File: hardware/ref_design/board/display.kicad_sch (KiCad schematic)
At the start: 12 parts, among them J3 FH12-50S-0.5SH(55), U6 AP3156FVG-7

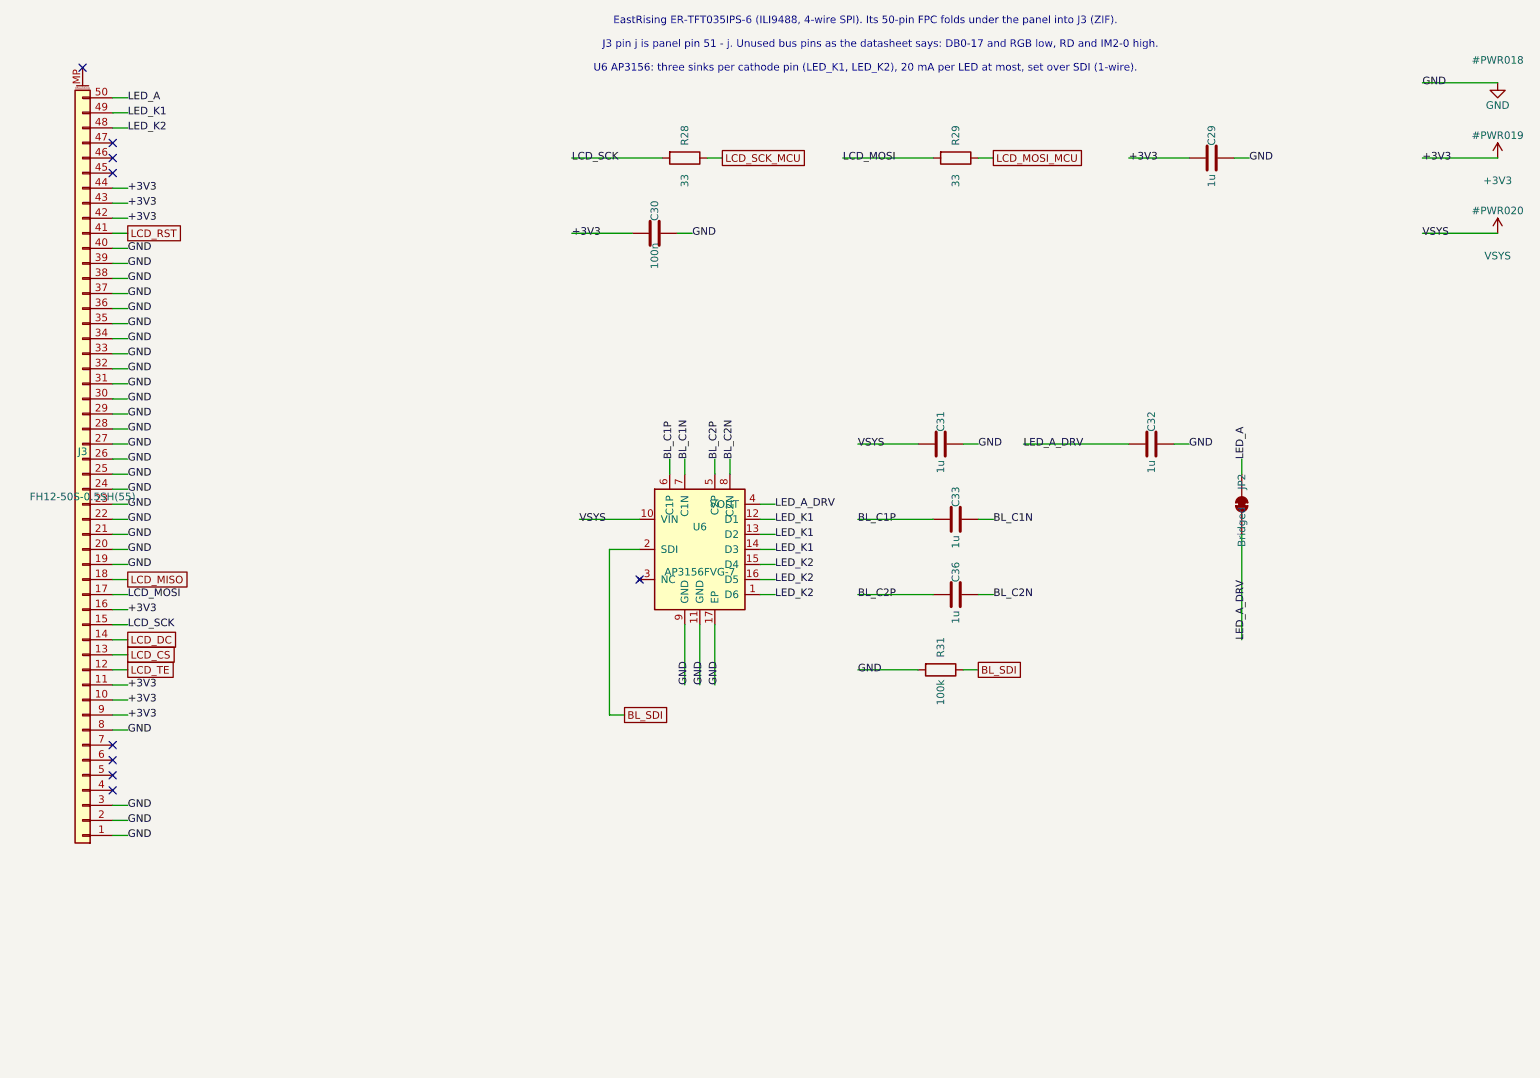
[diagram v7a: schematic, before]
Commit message: Reference design: discrete backlight current sinks replace the AP3156
The AP3156 charge pump (U6, C443652) is out of stock at JLC and LCSC. Each
of the panel's two cathode pins now has its own linear current sink: half
of an MCP6002 (U6, C7377 Preferred) drives an AO3400A (Q5/Q6, C20917 Basic)
and holds a 2.2 ohm sense resistor (R52/R53) at BL_REF. LED_A is on VSYS
through JP2. GPIO44 (now BL_PWM, PWM10 A) sets BL_REF through 100k/3.9k
and 1 uF: 0.124 V at 100% = 56 mA a pin, 113 mA in all (panel max 120).
RG 330 ohm, RF 10k, CF 1 nF, gate pull-downs 100k: simulated first
(board/sim, previous commit), phase margin >= 72.5 deg at every corner.

Every new part is Basic or Preferred: 12 extended part numbers instead of
13, parts $4.77 a board instead of $5.01, about $16.81 a unit at 10.

Layout: the sinks sit above J3's LED pins between J3 and J2, clear of the
ground bar route.py lays over J3's grounded pins; board rebuilt and
re-routed (route.py, 80 passes): DRC 0 errors, 0 unconnected, 0 parity,
2 cosmetic warnings as before. check_netlist, check_pins (29 parts, 244
pins, 94 passives), ERC 0, check_fit pass. silk.py puts J2's BATT label
above it (the op-amp is now on its left).

Docs: pin reviews for U6 and Q5/Q6 with page cites, passives, U4 (GPIO44)
and the panel; pinmap (GPIO44 PWM, backlight section), bring-up step 5,
design review, PLAN (also: the USB series resistors are 27 ohm, not 22),
BOM, assembly, validation plan items, SOURCES.

Co-Authored-By: Claude Opus 5.5 <noreply@anthropic.com>
Claude-Session: https://claude.ai/code/session_01Ceq1EsbekLwXHokcQ73Ldk
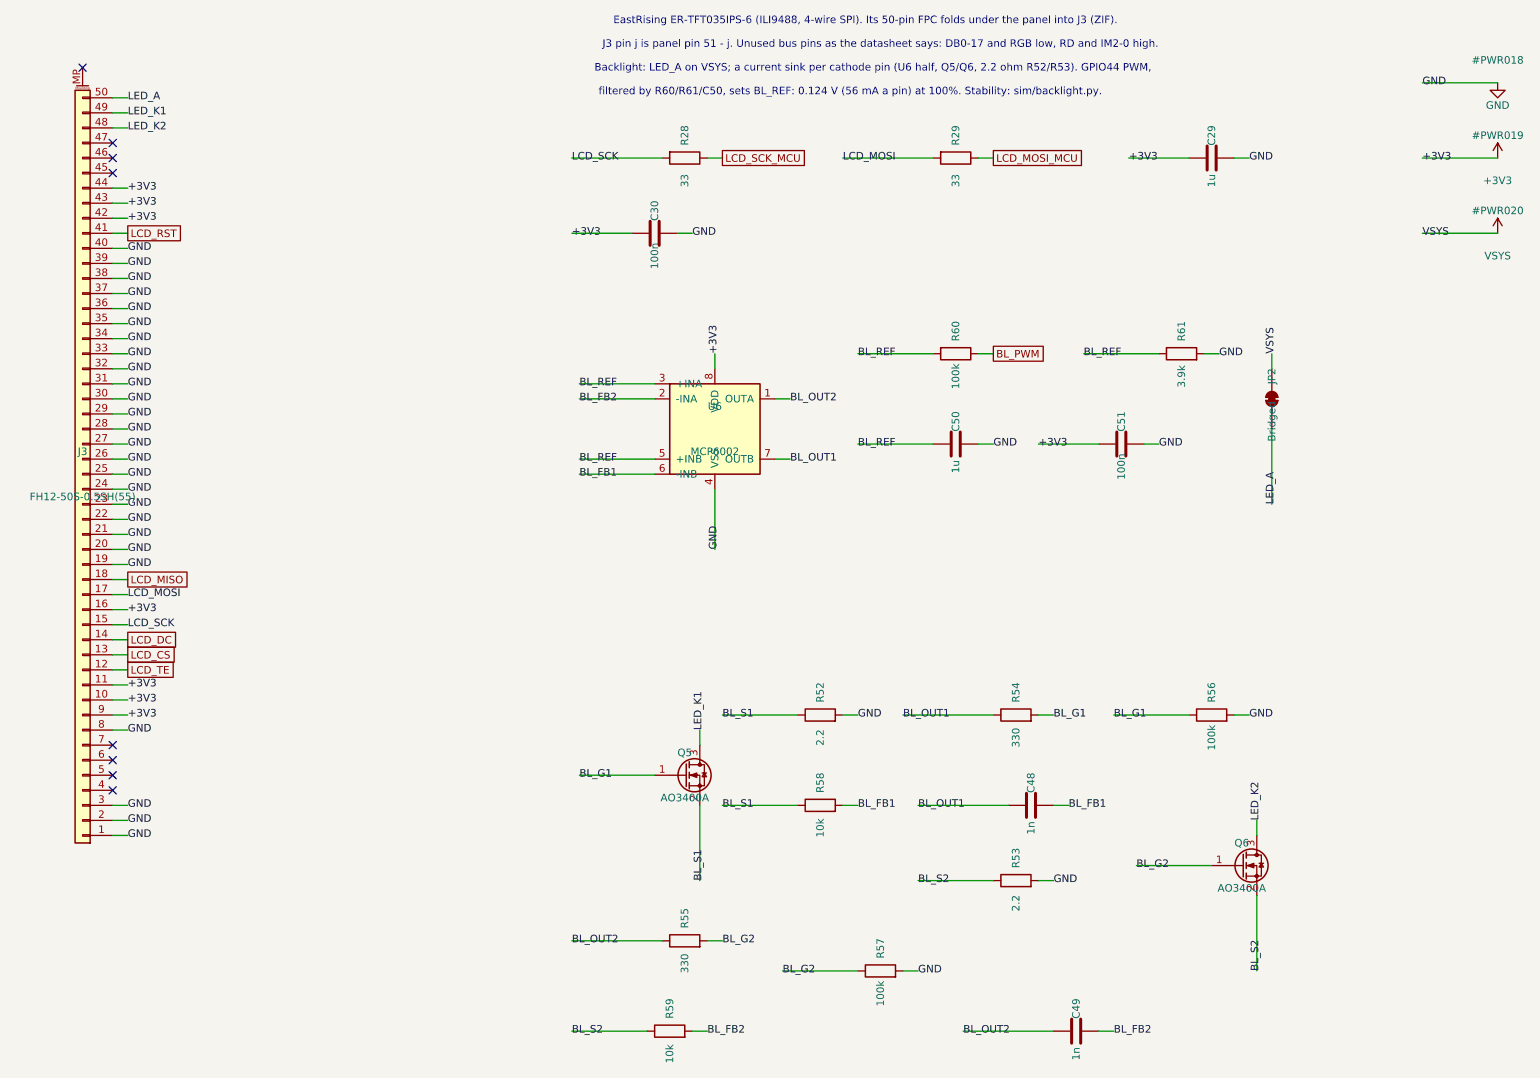
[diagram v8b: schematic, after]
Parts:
- removed C31, C32, C33, C36: 1u, Capacitor_SMD:C_0402_1005Metric, symbol Device:C
- removed R31: 100k, Resistor_SMD:R_0402_1005Metric, symbol Device:R
- removed U6: AP3156FVG-7, Package_DFN_QFN:QFN-16-1EP_4x4mm_P0.65mm_EP2.5x2.5mm_ThermalVias, symbol battler:AP3156
- added C48, C49: 1n, Capacitor_SMD:C_0402_1005Metric, symbol Device:C
- added C50: 1u, Capacitor_SMD:C_0402_1005Metric, symbol Device:C
- added C51: 100n, Capacitor_SMD:C_0402_1005Metric, symbol Device:C
- added Q5, Q6: AO3400A, Package_TO_SOT_SMD:SOT-23, symbol Transistor_FET:Q_NMOS_GSD
- added R52, R53: 2.2, Resistor_SMD:R_0603_1608Metric, symbol Device:R
- added R54, R55: 330, Resistor_SMD:R_0402_1005Metric, symbol Device:R
- added R56, R57, R60: 100k, Resistor_SMD:R_0402_1005Metric, symbol Device:R
- added R58, R59: 10k, Resistor_SMD:R_0402_1005Metric, symbol Device:R
- added R61: 3.9k, Resistor_SMD:R_0402_1005Metric, symbol Device:R
- added U6: MCP6002, Package_SO:SOIC-8_3.9x4.9mm_P1.27mm, symbol battler:MCP6002
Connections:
- net LED_A_DRV is gone; now on net VSYS: JP2.1 (A)
- net +3V3: now also C51.1, U6.8 (VDD)
- net GND: now also C50.2, C51.2, R52.2, R53.2, R56.2, R57.2, R61.2, U6.4 (VSS)
- net LED_K1: now also Q5.3 (D)
- net LED_K2: now also Q6.3 (D)
- new net BL_FB1: C48.2, R58.2, U6.6 (-INB)
- new net BL_FB2: C49.2, R59.2, U6.2 (-INA)
- new net BL_G1: Q5.1 (G), R54.2, R56.1
- new net BL_G2: Q6.1 (G), R55.2, R57.1
- new net BL_OUT1: C48.1, R54.1, U6.7 (OUTB)
- new net BL_OUT2: C49.1, R55.1, U6.1 (OUTA)
- new net BL_PWM: R60.1
- new net BL_REF: C50.1, R60.2, R61.1, U6.3 (+INA), U6.5 (+INB)
- new net BL_S1: Q5.2 (S), R52.1, R58.1
- new net BL_S2: Q6.2 (S), R53.1, R59.1
- no-connect marks 9 -> 8
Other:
- note added: "Backlight: LED_A on VSYS; a current sink per cathode pin (U6 half, Q5/Q6, 2.2 ohm R52/R53). GPIO44 PWM,"
- note added: "filtered by R60/R61/C50, sets BL_REF: 0.124 V (56 mA a pin) at 100%. Stability: sim/backlight.py."
- note removed: "U6 AP3156: three sinks per cathode pin (LED_K1, LED_K2), 20 mA per LED at most, set over SDI (1-wire)."
